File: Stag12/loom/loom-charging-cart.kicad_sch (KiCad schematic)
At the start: 50 parts, among them J1 523-2CMA193122R1000, J2 Conn_01x08_Pin, J38 Conn_01x04_Pin, J39 Conn_01x04_Pin, J40 Conn_01x08_Pin, J41 TSAL, J42 LATCHING, J43 POWER, J44 LATCHING, J45 Conn_01x02_Pin, J46 Conn_01x02_Pin, J47 Conn_01x02_Pin, J48 Conn_01x02_Pin, J49 Conn_01x02_Pin, J50 Conn_01x02_Pin, J51 Conn_01x02_Pin, J52 523-2CMA193122R1000, J53 Banana Plug, J54 Banana Plug, K1 Relay_DPST-NO, K2 Relay_DPST-NO, SW1 E-Stop, SW11 SW_DPST, SW14 SW_DPST, SW15 Close AIRs, SW16 Latching Reset, SW17 E-Stop, SW18 SW_DPST, SW19 SW_DPST, SW2 Latching Reset, SW3 Close AIRs

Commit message: Finish up charging cart loom
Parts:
- removed BT1: ACCU, symbol Device:Battery
- removed CB1: RS PRO DHMZ, symbol Device:CircuitBreaker_1P
- removed Conn1, Conn4: Molex_2x1P_Horizontal_THT, symbol Connectors_SUFST:Molex_2x1P_Horizontal_THT
- removed Conn5, Conn6: Molex_2x2P_Horizontal, symbol Connectors_SUFST:Molex_2x2P_Horizontal
- removed Conn57: AMPHENOL-47P-Pannel, symbol Connectors_SUFST:AMPHENOL-47P-Pannel
- removed D1: IMD Fault, symbol Device:LED
- removed D2: BMS Fault, symbol Device:LED
- removed D5: mains power, symbol Device:LED
- removed DZ1: MMSZ4701, PCM_Diode_SMD_AKL:D_SOD-123, symbol PCM_Diode_Zener_AKL:MMSZ4701
- removed J1: 523-2CMA193122R1000, symbol Connector_Generic:Conn_01x03
- removed K1: Relay_DPST-NO, symbol Relay:Relay_DPST-NO
- removed R2: R, symbol Device:R
- removed SW1: E-Stop, symbol Switch:SW_Push_Open
- removed SW11, SW14: SW_DPST, symbol Switch:SW_DPST
- removed SW2: Latching Reset, symbol Switch:SW_Push
- removed SW3: Close AIRs, symbol Switch:SW_SPST
- added CB1: RCBO 32ADP30CAT, symbol Device:CircuitBreaker_2P
- added CB2: RCBO 6ADP30CAT, symbol Device:CircuitBreaker_2P
- added Conn100: AIL LED, symbol Connectors_SUFST:Molex_2x1S_Recepticle
- added D11: KBPC1506W, Diode_THT:Diode_Bridge_GeneSiC_KBPC_W, symbol Diode_Bridge:KBPC1506W
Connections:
- net ACCU.GND: no longer Conn65.3, Conn65.6, J40.4 (Pin_4), J40.6 (Pin_6), J42.12 (Pin_12), J44.10 (Pin_10)
- net INV.CLOSE.+AIR: no longer Conn65.1, Conn65.7, J2.3 (Pin_3), J2.4 (Pin_4), J42.1 (Pin_1), J44.12 (Pin_12), J44.6 (Pin_6)
- net MAINS_L_IN: now also CB1.2, CB2.2, D11.4
- net MAINS_N_IN: now also CB1.4, CB2.4, D11.2; no longer K2.13, SW19.3
- net at K2.23: now also CB1.1; no longer SW19.1
- removed net +12V: Conn65.17, Conn65.2, Conn65.34, Conn65.4, J40.1 (Pin_1), J40.2 (Pin_2), J40.3 (Pin_3)
- net CAN.S.HIGH renamed CAN.B.HIGH
- net CAN.S.LOW renamed CAN.B.LOW
- new net: CB1.3, K2.13
- new net: CB2.1, SW19.1
- new net: CB2.3, SW19.3
- new net ACCU.CHARGE.PWR: Conn65.17, Conn65.34, J40.3 (Pin_3)
- new net ACCU.PWR: Conn65.4, J40.2 (Pin_2)
- new net AIL.HV+: D11.1 (+)
- new net AIL.HV-: D11.3 (-)
- new net AIL.LED.+: Conn100.1
- new net AIL.LED.-: Conn100.2
- new net CHASSIS.GND: Conn65.6, J40.4 (Pin_4)
- new net INV.CLOSE.PCHG: Conn65.7, J2.4 (Pin_4)
- new net LATCHING.RESET-: J42.12 (Pin_12), J44.10 (Pin_10)
- new net SHUT.ACCU.CHARGE: J42.1 (Pin_1), J44.12 (Pin_12), J44.6 (Pin_6)
- new net SHUT.IN: Conn65.1, J2.3 (Pin_3)
- new net TSAL.GND: Conn65.3, J40.6 (Pin_6)
- new net TSAL.PWR: Conn65.2, J40.1 (Pin_1)
- no-connect marks 34 -> 27
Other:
- note added: "ACCU CAR SIGNALS"
- note added: "ACCU CHARGER SIGNALS"
- note added: "Charge Enable Signal Powered by SDC"
- note added: "Drawn by Adam Eastman"
- note added: "G7L-2A-T DC12"
- note added: "Mains Voltage Indicator using AIL need to rectify mains"
- note added: "RCBO good practice"
- note removed: "12V power suply"
- note removed: "?"
- note removed: "CAR"
- note removed: "Change to socket molex"
- note removed: "LRS-50F-12"
- note removed: "Need to check SHUTDOWN Circuit"
- note removed: "PANEL"
- note removed: "TODO: 12V PSU must be isolated with DPST switch (250V rated) Move Latching to bottom right of sheet"
- note removed: "switch"
- moved on the sheet: Conn65, D10, D7, D8, D9, DZ2, J2, J38, J39, J40, J41, J42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

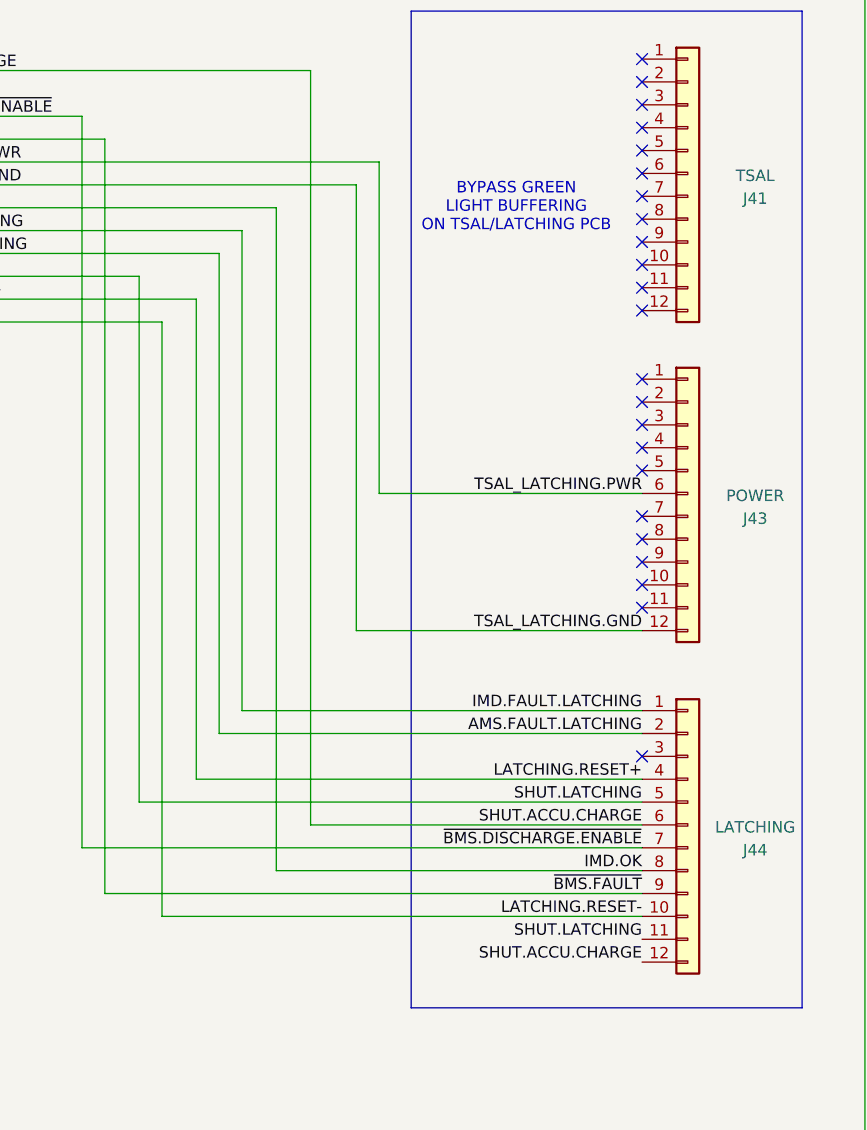
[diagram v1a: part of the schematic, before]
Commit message: Updated Pedal Box with new connectors
just one more autosport bro
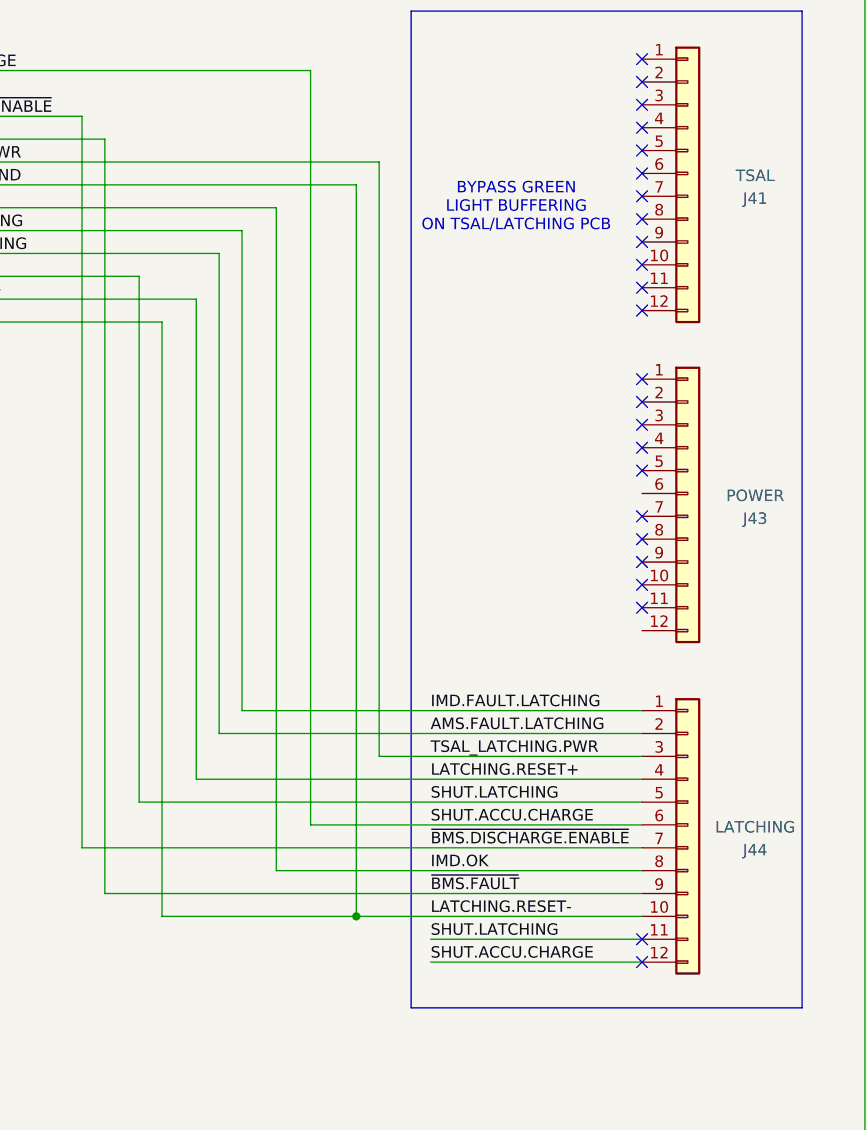
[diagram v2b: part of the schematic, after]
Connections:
- net LATCHING.RESET-: now also J42.6 (Pin_6)
- net TSAL_LATCHING.PWR: now also J44.3 (Pin_3); no longer J43.6 (Pin_6)
- net TSAL_LATCHING.GND: no longer names the net of J43.12 (Pin_12)
- net TSAL_LATCHING.GND: no longer J42.6 (Pin_6)
- no-connect marks 27 -> 28
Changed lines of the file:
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@@
 	)
 	(junction
+		(at 309.88 186.69)
+		(diameter 0)
+		(color 0 0 0 0)
+	)
+	(junction
 		(at 213.36 66.04)
 		(diameter 0)
@@
 	)
 	(no_connect
+		(at 341.63 189.23)
+	)
+	(no_connect
 		(at 341.63 134.62)
 	)
@@
 	)
 	(no_connect
+		(at 341.63 191.77)
+	)
+	(no_connect
 		(at 341.63 119.38)
 	)
@@
 	)
 	(no_connect
-		(at 341.63 168.91)
-	)
-	(no_connect
 		(at 341.63 91.44)
 	)
@@
 	(wire
 		(pts
-			(xy 341.63 171.45) (xy 292.1 171.45)
+			(xy 292.1 171.45) (xy 341.63 171.45)
 		)
 		(stroke
@@
 	(wire
 		(pts
+			(xy 309.88 186.69) (xy 341.63 186.69)
+		)
+		(stroke
+			(width 0)
+			(type default)
+		)
+	)
+	(wire
+		(pts
 			(xy 83.185 98.425) (xy 121.285 98.425)
 		)
@@
 	(wire
 		(pts
-			(xy 312.42 139.7) (xy 312.42 102.87)
+			(xy 312.42 102.87) (xy 312.42 168.91)
 		)
 		(stroke
@@
 	(wire
 		(pts
-			(xy 341.63 163.83) (xy 297.18 163.83)
+			(xy 297.18 163.83) (xy 341.63 163.83)
 		)
 		(stroke
@@
 	(wire
 		(pts
+			(xy 312.42 168.91) (xy 341.63 168.91)
+		)
+		(stroke
+			(width 0.5)
+			(type default)
+			(color 255 0 0 1)
+		)
+	)
+	(wire
+		(pts
 			(xy 131.445 88.265) (xy 83.185 88.265)
 		)
@@
 	(wire
 		(pts
-			(xy 341.63 139.7) (xy 312.42 139.7)
-		)
-		(stroke
-			(width 0.5)
-			(type default)
-			(color 255 0 0 1)
-		)
-	)
-	(wire
-		(pts
 			(xy 80.01 28.575) (xy 80.01 46.99)
 		)
@@
 	(wire
 		(pts
+			(xy 318.135 191.77) (xy 341.63 191.77)
+		)
+		(stroke
+			(width 0)
+			(type default)
+		)
+	)
+	(wire
+		(pts
 			(xy 83.185 131.445) (xy 113.665 131.445)
 		)
@@
 	(wire
 		(pts
+			(xy 318.135 189.23) (xy 341.63 189.23)
+		)
+		(stroke
+			(width 0)
+			(type default)
+		)
+	)
+	(wire
+		(pts
 			(xy 285.75 173.99) (xy 341.63 173.99)
 		)
@@
 	(wire
 		(pts
-			(xy 309.88 154.94) (xy 341.63 154.94)
-		)
-		(stroke
-			(width 0.5)
-			(type default)
-			(color 0 0 0 1)
-		)
-	)
-	(wire
-		(pts
 			(xy 112.395 142.875) (xy 112.395 172.085)
 		)
@@
 	(wire
 		(pts
-			(xy 288.29 186.69) (xy 341.63 186.69)
+			(xy 288.29 186.69) (xy 309.88 186.69)
 		)
 		(stroke
@@
 	(wire
 		(pts
-			(xy 309.88 105.41) (xy 309.88 154.94)
+			(xy 309.88 105.41) (xy 309.88 186.69)
 		)
 		(stroke
@@
 		)
 	)
-	(label "TSAL_LATCHING.PWR"
-		(at 341.63 139.7 180)
-		(effects
-			(font
-				(size 1.27 1.27)
-			)
-			(justify right bottom)
-		)
-	)
 	(label "ON.BUTTON.+"
 		(at 138.43 217.17 180)
@@
 	)
 	(label "SHUT.ACCU.CHARGE"
-		(at 341.63 191.77 180)
+		(at 318.135 191.77 0)
 		(effects
 			(font
 				(size 1.27 1.27)
 			)
-			(justify right bottom)
+			(justify left bottom)
 		)
 	)
@@
 	)
 	(label "SHUT.LATCHING"
-		(at 341.63 189.23 180)
+		(at 318.135 189.23 0)
 		(effects
 			(font
 				(size 1.27 1.27)
 			)
-			(justify right bottom)
+			(justify left bottom)
 		)
 	)
@@
 	)
 	(label "IMD.OK"
-		(at 341.63 181.61 180)
+		(at 318.135 181.61 0)
 		(effects
 			(font
 				(size 1.27 1.27)
 			)
-			(justify right bottom)
+			(justify left bottom)
 		)
 	)
@@
 	)
 	(label "SHUT.LATCHING"
-		(at 341.63 173.99 180)
+		(at 318.135 173.99 0)
 		(effects
 			(font
 				(size 1.27 1.27)
 			)
-			(justify right bottom)
+			(justify left bottom)
 		)
 	)
@@
 	)
 	(label "SHUT.ACCU.CHARGE"
-		(at 341.63 176.53 180)
+		(at 318.135 176.53 0)
 		(effects
 			(font
 				(size 1.27 1.27)
 			)
-			(justify right bottom)
+			(justify left bottom)
 		)
 	)
@@
 	)
 	(label "LATCHING.RESET-"
-		(at 341.63 186.69 180)
+		(at 318.135 186.69 0)
 		(effects
 			(font
 				(size 1.27 1.27)
 			)
-			(justify right bottom)
+			(justify left bottom)
 		)
 	)
@@
 	)
 	(label "AMS.FAULT.LATCHING"
-		(at 341.63 166.37 180)
+		(at 318.135 166.37 0)
 		(effects
 			(font
 				(size 1.27 1.27)
 			)
-			(justify right bottom)
+			(justify left bottom)
 		)
 	)
@@
 	)
 	(label "LATCHING.RESET+"
-		(at 341.63 171.45 180)
+		(at 318.135 171.45 0)
 		(effects
 			(font
 				(size 1.27 1.27)
 			)
-			(justify right bottom)
+			(justify left bottom)
 		)
 	)
@@
 	)
 	(label "IMD.FAULT.LATCHING"
-		(at 341.63 163.83 180)
+		(at 318.135 163.83 0)
 		(effects
 			(font
 				(size 1.27 1.27)
 			)
-			(justify right bottom)
+			(justify left bottom)
 		)
 	)
@@
 	)
 	(label "~{BMS.DISCHARGE.ENABLE}"
-		(at 341.63 179.07 180)
+		(at 318.135 179.07 0)
 		(effects
 			(font
 				(size 1.27 1.27)
 			)
-			(justify right bottom)
+			(justify left bottom)
 		)
 	)
@@
 		)
 	)
-	(label "TSAL_LATCHING.GND"
-		(at 341.63 154.94 180)
+	(label "INV.CLOSE.+AIR"
+		(at 159.385 93.345 180)
 		(effects
 			(font
@@
 		)
 	)
-	(label "INV.CLOSE.+AIR"
-		(at 159.385 93.345 180)
+	(label "TSAL_LATCHING.GND"
+		(at 254 105.41 0)
 		(effects
 			(font
 				(size 1.27 1.27)
 			)
-			(justify right bottom)
+			(justify left bottom)
 		)
 	)
-	(label "TSAL_LATCHING.GND"
-		(at 254 105.41 0)
+	(label "TSAL_LATCHING.PWR"
+		(at 318.135 168.91 0)
 		(effects
 			(font
@@
 	)
 	(label "~{BMS.FAULT}"
-		(at 341.63 184.15 180)
+		(at 318.135 184.15 0)
 		(effects
 			(font
 				(size 1.27 1.27)
 			)
-			(justify right bottom)
+			(justify left bottom)
 		)
 	)

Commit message: idfk
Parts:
- removed BT2: ACCU, symbol Device:Battery
- removed CB1: RCBO 32ADP30CAT, symbol Device:CircuitBreaker_2P
- removed CB2: RCBO 6ADP30CAT, symbol Device:CircuitBreaker_2P
- removed Conn100: AIL LED, symbol Connectors_SUFST:Molex_2x1S_Recepticle
- removed Conn65: AMPHENOL-47P-Pannel, symbol Connectors_SUFST:AMPHENOL-47P-Pannel
- removed D10: IMD FAULT, symbol Device:LED
- removed D11: KBPC1506W, Diode_THT:Diode_Bridge_GeneSiC_KBPC_W, symbol Diode_Bridge:KBPC1506W
- removed D7: POWER INDICATOR, symbol Device:LED
- removed D8: GREEN LIGHT, symbol Device:LED
- removed D9: AMS FAULT, symbol Device:LED
- removed DZ2: MMSZ4701, PCM_Diode_SMD_AKL:D_SOD-123, symbol PCM_Diode_Zener_AKL:MMSZ4701
- removed J2, J40: Conn_01x08_Pin, symbol Connector:Conn_01x08_Pin
- removed J38, J39: Conn_01x04_Pin, symbol Connector:Conn_01x04_Pin
- removed J41: TSAL, Connector_Molex:Molex_Micro-Fit_3.0_43045-1200_2x06_P3.00mm_Horizontal, symbol Connector_Generic:Conn_01x12
- removed J42, J44: LATCHING, Connector_Molex:Molex_Micro-Fit_3.0_43045-1200_2x06_P3.00mm_Horizontal, symbol Connector_Generic:Conn_01x12
- removed J43: POWER, Connector_Molex:Molex_Micro-Fit_3.0_43045-1200_2x06_P3.00mm_Horizontal, symbol Connector_Generic:Conn_01x12
- removed J45, J46, J47, J48, J49, J50, J51: Conn_01x02_Pin, symbol Connector:Conn_01x02_Pin
- removed J52: 523-2CMA193122R1000, symbol Connector_Generic:Conn_01x03
- removed J53, J54: Banana Plug, symbol Connector_Generic:Conn_01x01
- removed K2: Relay_DPST-NO, symbol Relay:Relay_DPST-NO
- removed SW15: Close AIRs, symbol Switch:SW_SPST
- removed SW16: Latching Reset, symbol Switch:SW_Push
- removed SW17: E-Stop, symbol Switch:SW_Push_Open
- removed SW18, SW19: SW_DPST, symbol Switch:SW_DPST
- added BT1: ACCU, symbol Device:Battery
- added Conn1, Conn4: Molex_2x1P_Horizontal_THT, symbol Connectors_SUFST:Molex_2x1P_Horizontal_THT
- added Conn5, Conn6: Molex_2x2P_Horizontal, symbol Connectors_SUFST:Molex_2x2P_Horizontal
- added Conn57: AMPHENOL-47P-Pannel, symbol Connectors_SUFST:AMPHENOL-47P-Pannel
- added D1: IMD Fault, symbol Device:LED
- added D2: BMS Fault, symbol Device:LED
- added D5: mains power, symbol Device:LED
- added DZ1: MMSZ4701, PCM_Diode_SMD_AKL:D_SOD-123, symbol PCM_Diode_Zener_AKL:MMSZ4701
- added J1: 523-2CMA193122R1000, symbol Connector_Generic:Conn_01x03
- added J2: CAN_S, symbol Connector:Conn_01x09_Pin
- added K1: Relay_DPST-NO, symbol Relay:Relay_DPST-NO
- added R2: R, symbol Device:R
- added SW1: E-Stop, symbol Switch:SW_Push_Open
- added SW11, SW14: SW_DPST, symbol Switch:SW_DPST
- added SW2: Latching Reset, symbol Switch:SW_Push
- added SW3: Close AIRs, symbol Switch:SW_SPST
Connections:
- net ACCU.GND: now also Conn4.2, Conn57.3, Conn57.5, Conn57.6, Conn6.2, SW2.1
- net BMS.CHARGER.SAFETY: now also Conn57.37
- net CAN.CHARGER.HIGH: now also Conn57.36
- net CAN.CHARGER.LOW: now also Conn57.35
- net GND: now also J1.3 (Pin_3), SW11.1, SW11.3
- net IMD.FAULT.LATCHING: now also Conn1.1, D1.1 (K)
- net IMD.OK: now also Conn5.3, Conn57.11
- net INV.CLOSE.+AIR: now also Conn57.1, Conn57.7, Conn57.8, Conn6.4
- net LATCHING.RESET+: now also Conn4.1, SW2.2
- net MAINS_L: now also K1.24, SW14.3
- net MAINS_L_IN: now also J1.1 (Pin_1), K1.23
- net MAINS_N: now also K1.14, SW14.1
- net MAINS_N_IN: now also J1.2 (Pin_2), K1.13
- net SHUT.LATCHING: now also Conn6.3, SW1.1 (A)
- net TS.ON: now also Conn57.9, SW3.1 (A)
- net TS.READY: now also Conn57.10
- net TSAL.GREEN.LIGHT: now also Conn57.13
- net ~{BMS.DISCHARGE.ENABLE}: now also Conn5.1, Conn57.16
- net ~{BMS.FAULT}: now also Conn5.2, Conn57.12
- net ~{CHARGE.ENABLE.INTERLOCKED}: now also Conn57.38
- new net: DZ1.1 (K), K1.A2
- new net: DZ1.2 (A), K1.A1, SW11.4
- new net: D5.1 (K), R2.1
- new net: R2.2, SW11.2
- new net +12V: Conn57.2, Conn57.34, Conn57.4, D1.2 (A), D2.2 (A), D5.2 (A), SW1.2 (B), SW3.2 (B)
- new net BMS.FAULT.LATCHING: Conn1.2, D2.1 (K)
- new net CAN.S.HIGH: Conn57.14, Conn57.18
- new net CAN.S.LOW: Conn57.15, Conn57.19
- new net EXC_SPLICE: Conn6.1
- new net SHUT.DISCHARGE: Conn57.17
- no-connect marks 28 -> 6
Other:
- note added: "12V power suply"
- note added: "?"
- note added: "CAR"
- note added: "Change to socket molex"
- note added: "LRS-50F-12"
- note added: "PANEL"
- note added: "TODO: 12V PSU must be isolated with DPST switch (250V rated) Move Latching to bottom right of sheet"
- note added: "switch"
- note removed: "12V power supply DRAN60-12(A) (Must be 12V out for BMS)"
- note removed: "ACCU CAR SIGNALS"
- note removed: "ACCU CHARGER SIGNALS"
- note removed: "BYPASS GREEN LIGHT BUFFERING ON TSAL/LATCHING PCB"
- note removed: "Charge Enable Signal Powered by SDC"
- note removed: "Drawn by Adam Eastman"
- note removed: "G7L-2A-T DC12"
- note removed: "MEASUREMENT POINTS"
- note removed: "Mains Voltage Indicator using AIL need to rectify mains"
- note removed: "Need to check BMS Charge Signals"
- note removed: "PANEL I/O"
- note removed: "RCBO good practice"

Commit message: Updates to charging cart loom
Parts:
- removed J2: CAN_S, symbol Connector:Conn_01x09_Pin
- added BT2: ACCU, symbol Device:Battery
- added Conn65: AMPHENOL-47P-Pannel, symbol Connectors_SUFST:AMPHENOL-47P-Pannel
- added D10: IMD FAULT, symbol Device:LED
- added D7: POWER INDICATOR, symbol Device:LED
- added D8: GREEN LIGHT, symbol Device:LED
- added D9: AMS FAULT, symbol Device:LED
- added DZ2: MMSZ4701, PCM_Diode_SMD_AKL:D_SOD-123, symbol PCM_Diode_Zener_AKL:MMSZ4701
- added J2, J40: Conn_01x08_Pin, symbol Connector:Conn_01x08_Pin
- added J38, J39: Conn_01x04_Pin, symbol Connector:Conn_01x04_Pin
- added J41: TSAL, Connector_Molex:Molex_Micro-Fit_3.0_43045-1200_2x06_P3.00mm_Horizontal, symbol Connector_Generic:Conn_01x12
- added J42, J44: LATCHING, Connector_Molex:Molex_Micro-Fit_3.0_43045-1200_2x06_P3.00mm_Horizontal, symbol Connector_Generic:Conn_01x12
- added J43: POWER, Connector_Molex:Molex_Micro-Fit_3.0_43045-1200_2x06_P3.00mm_Horizontal, symbol Connector_Generic:Conn_01x12
- added J45, J46, J47, J48, J49, J50, J51: Conn_01x02_Pin, symbol Connector:Conn_01x02_Pin
- added J52: 523-2CMA193122R1000, symbol Connector_Generic:Conn_01x03
- added K2: Relay_DPST-NO, symbol Relay:Relay_DPST-NO
- added SW15: Close AIRs, symbol Switch:SW_SPST
- added SW16: Latching Reset, symbol Switch:SW_Push
- added SW17: E-Stop, symbol Switch:SW_Push_Open
- added SW18, SW19: SW_DPST, symbol Switch:SW_DPST
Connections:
- net EXC_SPLICE is gone; now on net ACCU.GND: Conn6.1
- net TSAL.GREEN.LIGHT is gone; now on net SHUT.DISCHARGE: Conn57.13
- net +12V: now also Conn65.2, Conn65.34, Conn65.4, J40.1 (Pin_1), J40.2 (Pin_2), J40.3 (Pin_3)
- net ACCU.GND: now also Conn65.3, Conn65.5, Conn65.6, J40.4 (Pin_4), J40.5 (Pin_5), J40.6 (Pin_6), J42.12 (Pin_12), J44.10 (Pin_10)
- net BMS.CHARGER.SAFETY: now also Conn65.37
- net CAN.CHARGER.HIGH: now also Conn65.36, J39.3 (Pin_3), J40.8 (Pin_8)
- net CAN.CHARGER.LOW: now also Conn65.35, J39.4 (Pin_4), J40.7 (Pin_7)
- net CAN.S.HIGH: now also Conn65.14, Conn65.18
- net CAN.S.LOW: now also Conn65.15, Conn65.19
- net GND: now also J52.3 (Pin_3)
- net IMD.FAULT.LATCHING: now also J42.8 (Pin_8), J44.1 (Pin_1)
- net IMD.OK: now also Conn65.11, J2.8 (Pin_8), J42.7 (Pin_7), J44.8 (Pin_8)
- net INV.CLOSE.+AIR: now also Conn65.1, Conn65.7, Conn65.8, J2.3 (Pin_3), J2.4 (Pin_4), J2.5 (Pin_5), J42.1 (Pin_1), J44.12 (Pin_12), J44.6 (Pin_6)
- net LATCHING.RESET+: now also J42.11 (Pin_11), J44.4 (Pin_4)
- net MAINS_L: now also K2.24
- net MAINS_L_IN: now also J52.1 (Pin_1), K2.23, SW19.1
- net MAINS_N: now also K2.14
- net MAINS_N_IN: now also J52.2 (Pin_2), K2.13, SW19.3
- net SHUT.DISCHARGE: now also Conn65.13, Conn65.17
- net SHUT.LATCHING: now also J42.10 (Pin_10), J44.11 (Pin_11), J44.5 (Pin_5)
- net TS.ON: now also Conn65.9, J2.7 (Pin_7)
- net TS.READY: now also Conn65.10
- net ~{BMS.DISCHARGE.ENABLE}: now also Conn65.16, J2.1 (Pin_1), J42.3 (Pin_3), J44.7 (Pin_7)
- net ~{BMS.FAULT}: now also Conn65.12, J2.2 (Pin_2), J42.4 (Pin_4), J44.9 (Pin_9)
- net ~{CHARGE.ENABLE.INTERLOCKED}: now also Conn65.38
- new net: D9.1 (K), J49.2 (Pin_2)
- new net: D9.2 (A), J49.1 (Pin_1)
- new net: J51.1 (Pin_1), SW16.1
- new net: J51.2 (Pin_2), SW16.2
- new net: J47.1 (Pin_1), SW15.1 (A)
- new net: J47.2 (Pin_2), SW15.2 (B)
- new net: J50.1 (Pin_1), SW17.1 (A)
- new net: J50.2 (Pin_2), SW17.2 (B)
- new net: D8.1 (K), J46.2 (Pin_2)
- new net: D8.2 (A), J46.1 (Pin_1)
- new net: D7.2 (A), J45.1 (Pin_1)
- new net: D7.1 (K), J45.2 (Pin_2)
- new net: D10.2 (A), J48.1 (Pin_1)
- new net: D10.1 (K), J48.2 (Pin_2)
- new net AMS.FAULT.LATCHING: J42.9 (Pin_9), J44.2 (Pin_2)
- new net CHARGER.ON: DZ2.2 (A), J39.1 (Pin_1), K2.A1
- new net MAINS.RELAY.CLOSE: DZ2.1 (K), J39.2 (Pin_2), K2.A2
- new net ON.BUTTON.+: J38.2 (Pin_2), SW18.4
- new net ON.BUTTON.-: J38.1 (Pin_1), SW18.3
- new net ON.BUTTON.LED.+: J38.4 (Pin_4), SW18.2
- new net ON.BUTTON.LED.-: J38.3 (Pin_3), SW18.1
- new net TSAL_LATCHING.GND: J42.6 (Pin_6), J43.12 (Pin_12)
- new net TSAL_LATCHING.PWR: J42.5 (Pin_5), J43.6 (Pin_6)
- no-connect marks 6 -> 32
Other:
- note added: "12V power supply DRAN60-12(A)"
- note added: "BYPASS GREEN LIGHT BUFFERING ON TSAL/LATCHING PCB"
- note added: "PANEL I/O"
- moved on the sheet: Conn57, DZ1, J1, SW11, SW14
